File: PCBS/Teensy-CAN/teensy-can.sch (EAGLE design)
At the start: 12 parts

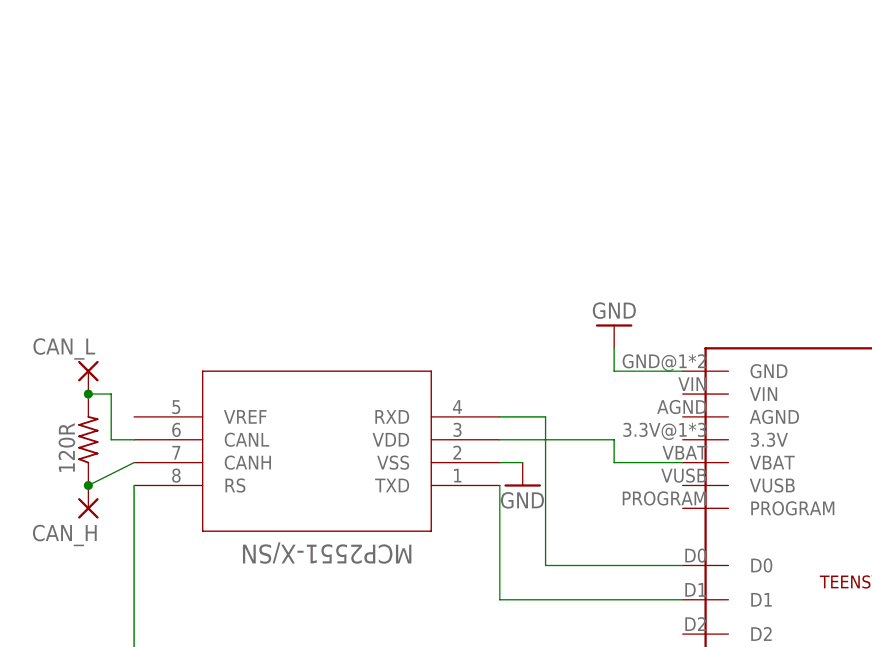
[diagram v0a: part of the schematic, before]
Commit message: Adding DC-DC to control board. UNFINISHED
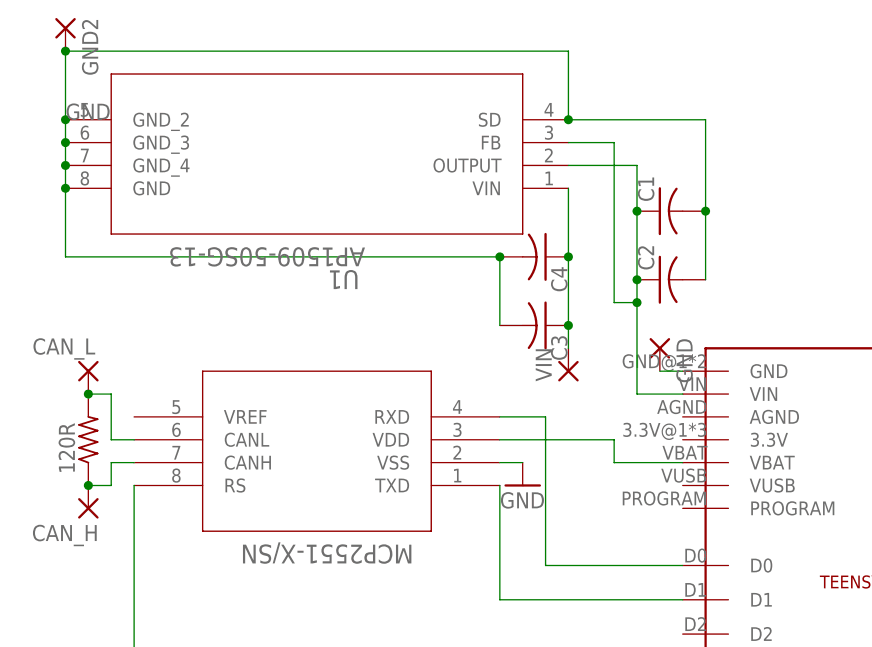
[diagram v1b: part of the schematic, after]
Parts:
- added C1, C2, C3, C4: (no value), rcl:C-USC0402
- added GND, GND2, VIN: (no value), wirepad:1,6/0,8
- added U1: AP1509-50SG-13, AP150950SG13:AP1509-50SG-13
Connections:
- new net N$10: GND.P, U$2.GND
- new net N$11: C3.1, C4.1, U1.VIN, VIN.P
- new net N$12: C1.1, C2.1, U$2.VIN, U1.FB, U1.OUTPUT
- net GND: now also C1.2, C2.2, C3.2, C4.2, GND2.P, U1.GND, U1.GND_2, U1.GND_3, U1.GND_4, U1.SD; no longer U$2.GND

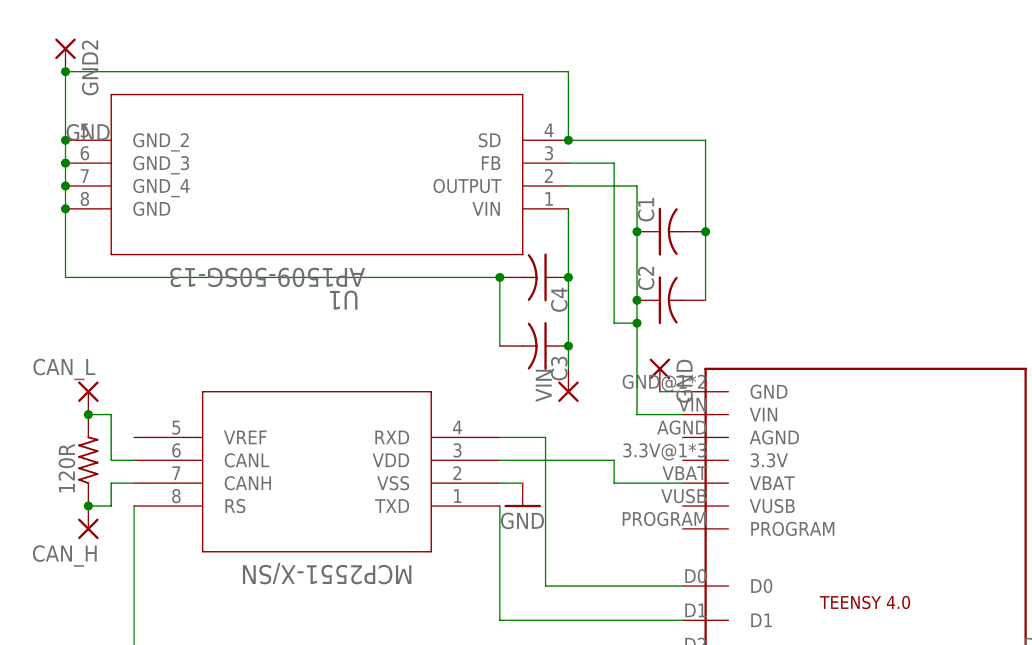
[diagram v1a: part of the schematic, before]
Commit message: teensy board final draft
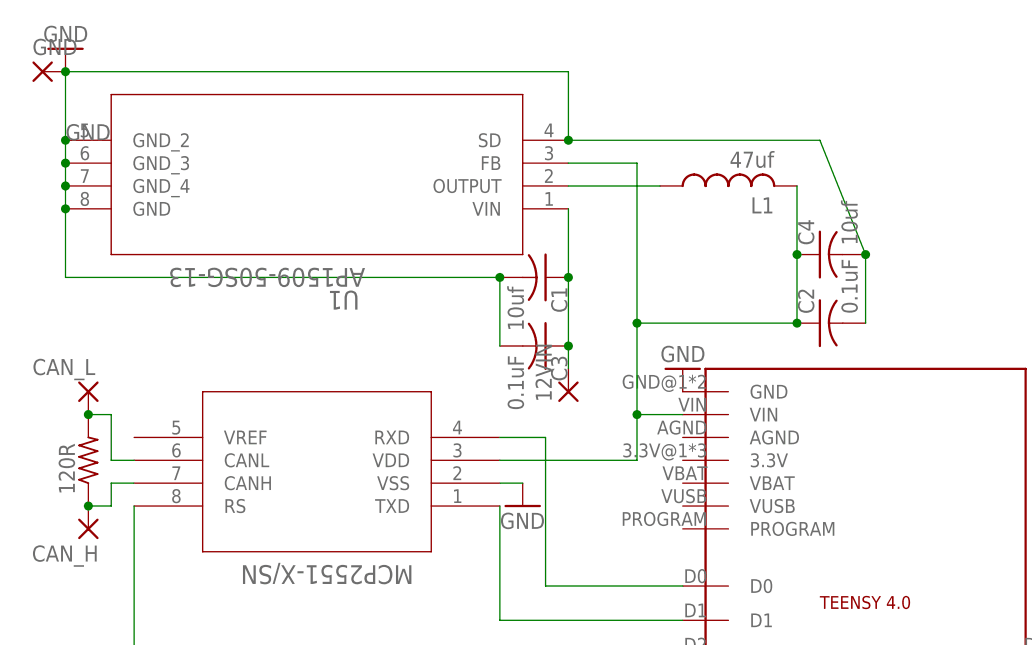
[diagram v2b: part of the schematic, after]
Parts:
- removed GND2: (no value), wirepad:1,6/0,8
- added L1: 47uf, rcl:L-US0207/7
- C1, C4: value (none) -> 10uf; device rcl:C-USC0402 -> rcl:C-US050-024X044
- C2, C3: value (none) -> 0.1uF
- renumbered VIN to 12VIN
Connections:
- removed net N$10: GND.P, U$2.GND
- removed net N$11: 12VIN.P, C3.1, C4.1, U1.VIN
- removed net N$12: C1.1, C2.1, U$2.VIN, U1.FB, U1.OUTPUT
- removed net VBAT: U$1.VDD, U$2.VBAT
- new net 12VIN: 12VIN.P, C1.1, C3.1, U1.VIN
- new net 5VIN: C2.1, C4.1, L1.2, U$1.VDD, U$2.VIN, U1.FB
- new net OUTPUT: L1.1, U1.OUTPUT
- net GND: now also GND.P, U$2.GND; no longer GND2.P
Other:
- moved on the sheet: C1, C2, C4, GND

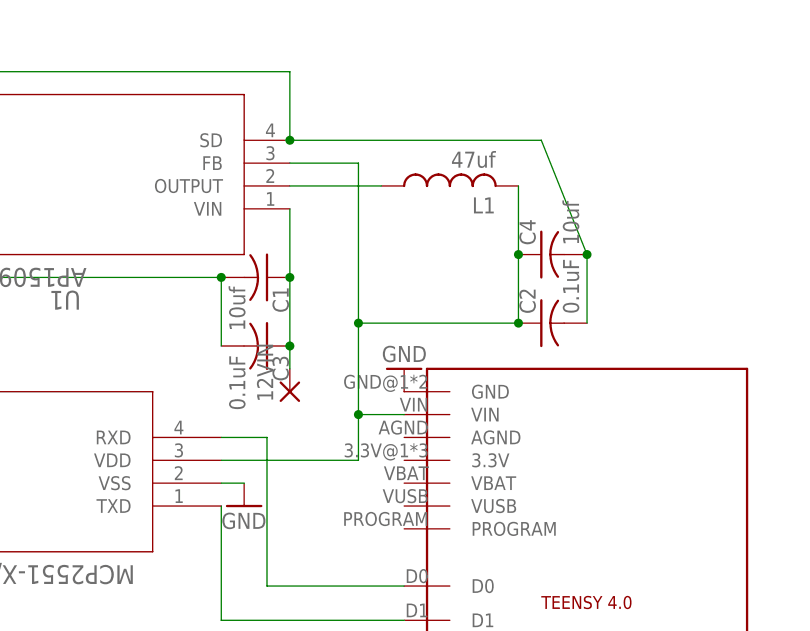
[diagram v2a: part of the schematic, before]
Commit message: charger and board changes, adding firmware soon
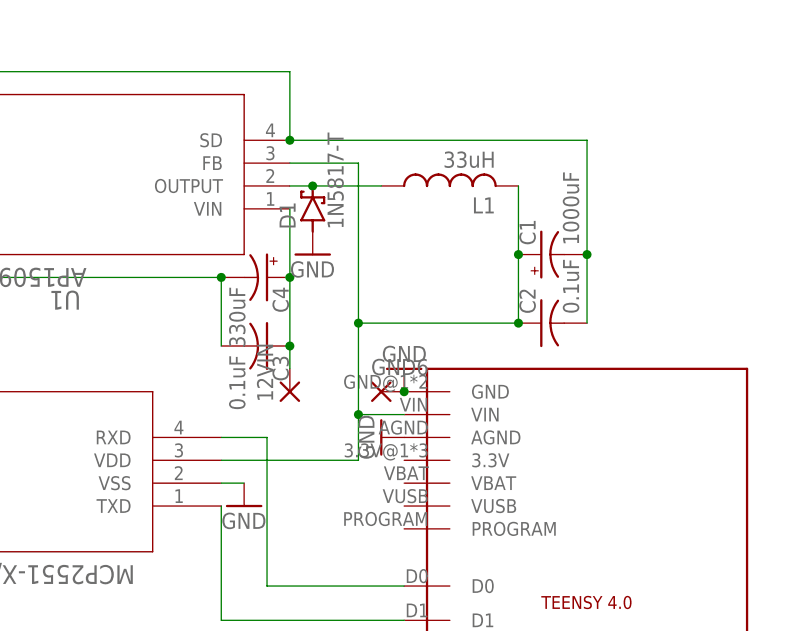
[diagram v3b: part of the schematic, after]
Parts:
- added D1: 1N5817-T, diode:1N5817-T
- added GND6: (no value), wirepad:1,6/0,8
- C1: value 10uf -> 1000uF; device rcl:C-US050-024X044 -> rcl:CPOL-USE5-10.5
- C4: value 10uf -> 330uF; device rcl:C-US050-024X044 -> rcl:CPOL-USE3.5-8
- L1: value 47uf -> 33uH; device rcl:L-US0207/7 -> rcl:L-USL2012C
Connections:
- net 12VIN: now also C4.+; no longer C1.1
- net 5VIN: now also C1.+; no longer C4.1
- net GND: now also C1.-, C4.-, D1.A, GND6.P, U$2.AGND; no longer C1.2, C4.2
- net OUTPUT: now also D1.C
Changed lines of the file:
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@@
 <part name="GND2" library="supply1" library_urn="urn:adsk.eagle:library:371" deviceset="GND" device=""/>
 <part name="GND3" library="supply1" library_urn="urn:adsk.eagle:library:371" deviceset="GND" device=""/>
-<part name="C1" library="rcl" library_urn="urn:adsk.eagle:library:334" deviceset="C-US" device="050-024X044" package3d_urn="urn:adsk.eagle:package:23643/1" value="10uf"/>
-<part name="C4" library="rcl" library_urn="urn:adsk.eagle:library:334" deviceset="C-US" device="050-024X044" package3d_urn="urn:adsk.eagle:package:23643/1" value="10uf"/>
-<part name="L1" library="rcl" library_urn="urn:adsk.eagle:library:334" deviceset="L-US" device="0207/7" package3d_urn="urn:adsk.eagle:package:23493/2" value="47uf"/>
+<part name="GND4" library="supply1" library_urn="urn:adsk.eagle:library:371" deviceset="GND" device=""/>
+<part name="GND5" library="supply1" library_urn="urn:adsk.eagle:library:371" deviceset="GND" device=""/>
+<part name="C1" library="rcl" library_urn="urn:adsk.eagle:library:334" deviceset="CPOL-US" device="E5-10.5" package3d_urn="urn:adsk.eagle:package:23372/2" value="1000uF"/>
+<part name="L1" library="rcl" library_urn="urn:adsk.eagle:library:334" deviceset="L-US" device="L2012C" package3d_urn="urn:adsk.eagle:package:23475/2" value="33uH"/>
+<part name="D1" library="diode" library_urn="urn:adsk.eagle:library:210" deviceset="1N581*" device="" package3d_urn="urn:adsk.eagle:package:43421/1" technology="7-T"/>
+<part name="GND6" library="wirepad" library_urn="urn:adsk.eagle:library:412" deviceset="1,6/0,8" device="" package3d_urn="urn:adsk.eagle:package:30830/1"/>
+<part name="C4" library="rcl" library_urn="urn:adsk.eagle:library:334" deviceset="CPOL-US" device="E3.5-8" package3d_urn="urn:adsk.eagle:package:23360/2" value="330uF"/>
 </parts>
 <sheets>
@@
 <attribute name="VALUE" x="50.8" y="68.58" size="1.778" layer="96" rot="R180"/>
 </instance>
-<instance part="C1" gate="G$1" x="33.02" y="76.2" smashed="yes" rot="R270">
-<attribute name="NAME" x="33.655" y="75.184" size="1.778" layer="95" rot="R270"/>
-<attribute name="VALUE" x="28.829" y="75.184" size="1.778" layer="96" rot="R270"/>
-</instance>
-<instance part="C4" gate="G$1" x="63.5" y="78.74" smashed="yes" rot="R90">
+<instance part="GND4" gate="1" x="45.72" y="58.42" smashed="yes" rot="R270">
+<attribute name="VALUE" x="43.18" y="60.96" size="1.778" layer="96" rot="R270"/>
+</instance>
+<instance part="GND5" gate="1" x="38.1" y="78.74" smashed="yes">
+<attribute name="VALUE" x="35.56" y="76.2" size="1.778" layer="96"/>
+</instance>
+<instance part="C1" gate="G$1" x="63.5" y="78.74" smashed="yes" rot="R90">
 <attribute name="NAME" x="62.865" y="79.756" size="1.778" layer="95" rot="R90"/>
 <attribute name="VALUE" x="67.691" y="79.756" size="1.778" layer="96" rot="R90"/>
@@
 <attribute name="NAME" x="58.42" y="85.09" size="1.778" layer="95" rot="R180"/>
 <attribute name="VALUE" x="58.42" y="90.17" size="1.778" layer="96" rot="R180"/>
+</instance>
+<instance part="D1" gate="G$1" x="38.1" y="83.82" smashed="yes" rot="R90">
+<attribute name="NAME" x="36.195" y="81.534" size="1.778" layer="95" rot="R90"/>
+<attribute name="VALUE" x="41.529" y="81.534" size="1.778" layer="96" rot="R90"/>
+</instance>
+<instance part="GND6" gate="P" x="45.72" y="63.5" smashed="yes">
+<attribute name="NAME" x="44.577" y="65.3542" size="1.778" layer="95"/>
+<attribute name="VALUE" x="44.577" y="60.198" size="1.778" layer="96"/>
+</instance>
+<instance part="C4" gate="G$1" x="33.02" y="76.2" smashed="yes" rot="R270">
+<attribute name="NAME" x="33.655" y="75.184" size="1.778" layer="95" rot="R270"/>
+<attribute name="VALUE" x="28.829" y="75.184" size="1.778" layer="96" rot="R270"/>
 </instance>
 </instances>
@@
 <pinref part="C3" gate="G$1" pin="2"/>
 <wire x1="27.94" y1="68.58" x2="27.94" y2="76.2" width="0.1524" layer="91"/>
-<pinref part="C2" gate="G$1" pin="2"/>
-<wire x1="68.58" y1="71.12" x2="68.58" y2="78.74" width="0.1524" layer="91"/>
 <pinref part="U1" gate="A" pin="GND_2"/>
 <pinref part="U1" gate="A" pin="GND_3"/>
@@
 <wire x1="-20.32" y1="99.06" x2="-20.32" y2="91.44" width="0.1524" layer="91"/>
 <junction x="-20.32" y="91.44"/>
-<wire x1="68.58" y1="78.74" x2="63.5" y2="91.44" width="0.1524" layer="91"/>
-<wire x1="63.5" y1="91.44" x2="35.56" y2="91.44" width="0.1524" layer="91"/>
+<wire x1="68.58" y1="91.44" x2="35.56" y2="91.44" width="0.1524" layer="91"/>
 <junction x="35.56" y="91.44"/>
 <wire x1="27.94" y1="76.2" x2="-20.32" y2="76.2" width="0.1524" layer="91"/>
@@
 <pinref part="GND2" gate="1" pin="GND"/>
 <junction x="-20.32" y="99.06"/>
-<pinref part="C1" gate="G$1" pin="2"/>
+<pinref part="GND" gate="P" pin="P"/>
+<pinref part="C2" gate="G$1" pin="2"/>
+<wire x1="68.58" y1="71.12" x2="68.58" y2="78.74" width="0.1524" layer="91"/>
+<pinref part="C1" gate="G$1" pin="-"/>
+<wire x1="68.58" y1="91.44" x2="68.58" y2="78.74" width="0.1524" layer="91"/>
+<junction x="68.58" y="78.74"/>
+<pinref part="C4" gate="G$1" pin="-"/>
 <junction x="27.94" y="76.2"/>
-<pinref part="C4" gate="G$1" pin="2"/>
-<junction x="68.58" y="78.74"/>
-<pinref part="GND" gate="P" pin="P"/>
 </segment>
 <segment>
 <pinref part="U$2" gate="G$1" pin="GND"/>
 <pinref part="GND3" gate="1" pin="GND"/>
+<pinref part="GND6" gate="P" pin="P"/>
+<junction x="48.26" y="63.5"/>
+</segment>
+<segment>
+<pinref part="U$2" gate="G$1" pin="AGND"/>
+<pinref part="GND4" gate="1" pin="GND"/>
+</segment>
+<segment>
+<pinref part="GND5" gate="1" pin="GND"/>
+<pinref part="D1" gate="G$1" pin="A"/>
 </segment>
 </net>
@@
 <pinref part="U$2" gate="G$1" pin="VIN"/>
 <wire x1="43.18" y1="60.96" x2="48.26" y2="60.96" width="0.1524" layer="91"/>
+<pinref part="C2" gate="G$1" pin="1"/>
 <wire x1="60.96" y1="86.36" x2="60.96" y2="78.74" width="0.1524" layer="91"/>
-<pinref part="C2" gate="G$1" pin="1"/>
 <wire x1="60.96" y1="78.74" x2="60.96" y2="71.12" width="0.1524" layer="91"/>
 <wire x1="60.96" y1="71.12" x2="43.18" y2="71.12" width="0.1524" layer="91"/>
@@
 <pinref part="U1" gate="A" pin="FB"/>
 <wire x1="35.56" y1="88.9" x2="43.18" y2="88.9" width="0.1524" layer="91"/>
+<pinref part="C1" gate="G$1" pin="+"/>
+<junction x="60.96" y="78.74"/>
 <wire x1="43.18" y1="88.9" x2="43.18" y2="71.12" width="0.1524" layer="91"/>
-<pinref part="C4" gate="G$1" pin="1"/>
-<junction x="60.96" y="78.74"/>
 <pinref part="L1" gate="G$1" pin="2"/>
 </segment>
@@
 <junction x="35.56" y="68.58"/>
 <wire x1="35.56" y1="68.58" x2="35.56" y2="76.2" width="0.1524" layer="91"/>
-<pinref part="C1" gate="G$1" pin="1"/>
+<pinref part="C4" gate="G$1" pin="+"/>
 <wire x1="35.56" y1="76.2" x2="35.56" y2="83.82" width="0.1524" layer="91"/>
 <junction x="35.56" y="76.2"/>
@@
 <segment>
 <pinref part="U1" gate="A" pin="OUTPUT"/>
-<wire x1="35.56" y1="86.36" x2="45.72" y2="86.36" width="0.1524" layer="91"/>
 <pinref part="L1" gate="G$1" pin="1"/>
+<wire x1="35.56" y1="86.36" x2="38.1" y2="86.36" width="0.1524" layer="91"/>
+<pinref part="D1" gate="G$1" pin="C"/>
+<wire x1="38.1" y1="86.36" x2="45.72" y2="86.36" width="0.1524" layer="91"/>
+<junction x="38.1" y="86.36"/>
 </segment>
 </net>
@@
 </sheet>
 </sheets>
+<errors>
+</errors>
 </schematic>
 </drawing>
